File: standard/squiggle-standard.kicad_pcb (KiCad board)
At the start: 2 copper layers, 116 x 101.2 mm, 38 parts, among them SW1 switch, SW10 switch, SW11 switch, SW12 switch, SW13 switch, SW14 switch, SW15 switch, SW16 switch, SW17 switch, SW2 switch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

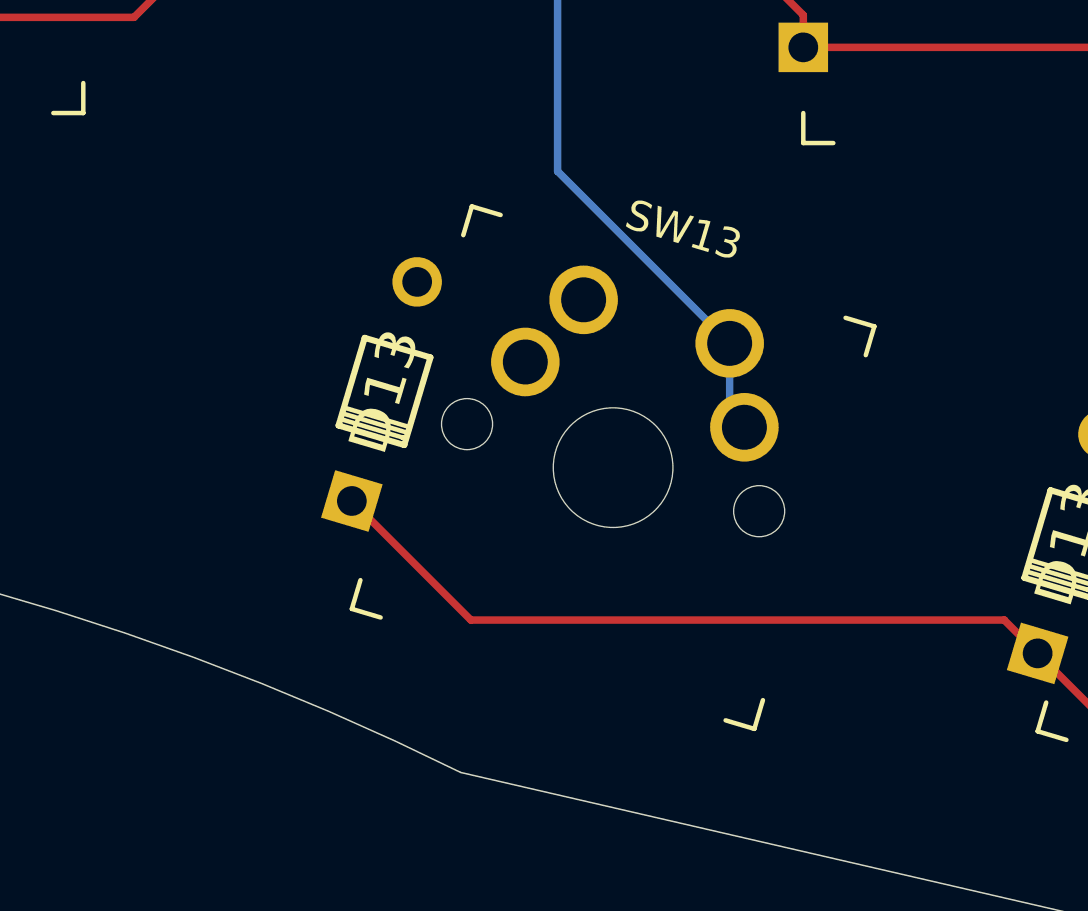
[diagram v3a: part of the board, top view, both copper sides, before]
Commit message: replaced switch with encoder
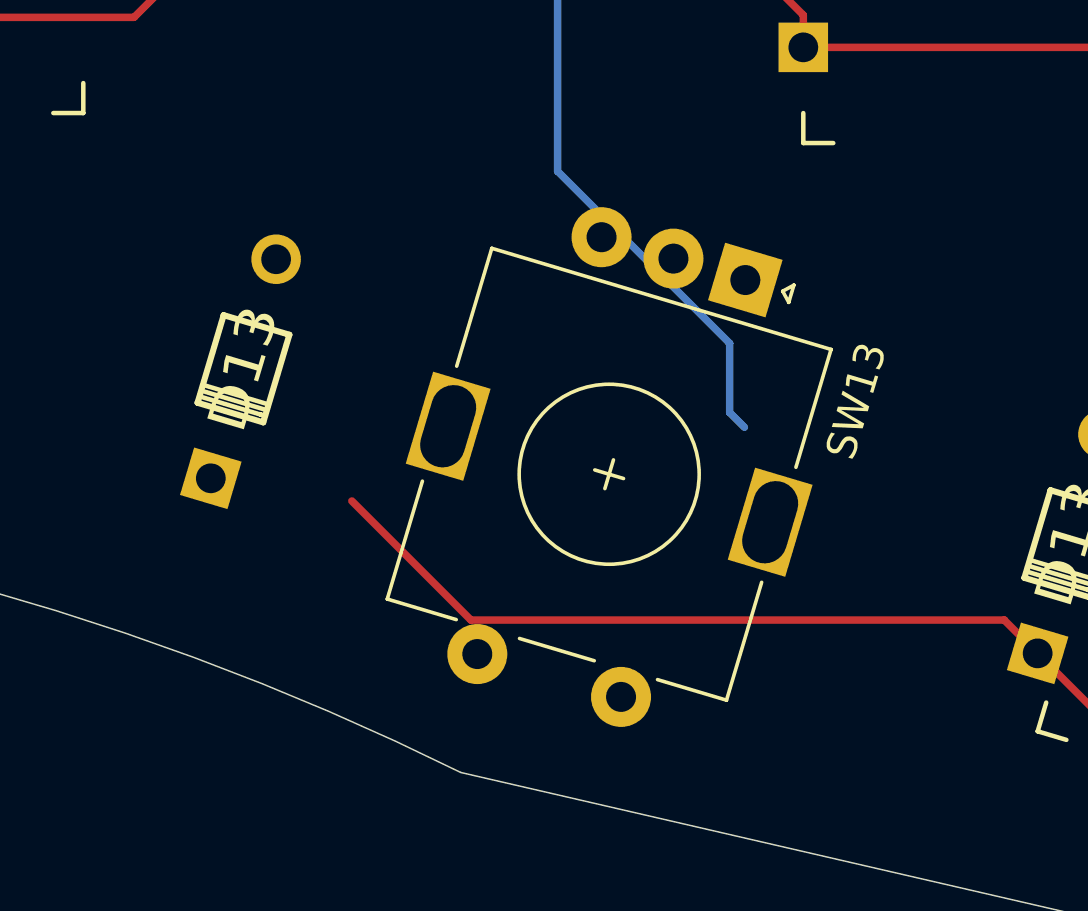
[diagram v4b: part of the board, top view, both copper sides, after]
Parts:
- SW13: footprint footprints:SW_MX_reversible -> Rotary_Encoder:RotaryEncoder_Alps_EC11E-Switch_Vertical_H20mm
- moved SW13 7.65 mm to (78.1, 77.6), turned to -106.6 degrees
- moved D13 4.76 mm to (61.3, 80.5)
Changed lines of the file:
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@@
       (net 11 "Net-(D15-Pad2)"))
   )
-  (footprint "footprints:SW_MX_reversible" (layer "F.Cu")
-    (at 73.66 83.82 -16.6)
-    (descr "MX-style keyswitch, reversible")
-    (tags "MX,cherry,gateron,kailh")
+  (footprint "Rotary_Encoder:RotaryEncoder_Alps_EC11E-Switch_Vertical_H20mm" (layer "F.Cu")
+    (at 78.067048 77.566382 -106.6)
+    (descr "Alps rotary encoder, EC12E... with switch, vertical shaft, http://www.alps.com/prod/info/E/HTML/Encoder/Incremental/EC11/EC11E15204A3.html")
+    (tags "rotary encoder")
     (attr through_hole)
-    (fp_text reference "SW13" (at 0 -8.255 -16.6) (layer "F.SilkS")
+    (fp_text reference "SW13" (at 2.8 -4.7 73.4) (layer "F.SilkS")
       (effects (font (size 1 1) (thickness 0.15)))
     )
-    (fp_text value "switch" (at 0 8.255 -16.6) (layer "F.Fab")
+    (fp_text value "switch" (at 7.5 10.4 73.4) (layer "F.Fab")
       (effects (font (size 1 1) (thickness 0.15)))
     )
-    (fp_text user "${REFERENCE}" (at 0 -8.255 -16.6) (layer "B.SilkS")
+    (fp_text user "2.00u" (at -15.24 8.255 73.4) (layer "Dwgs.User")
+      (effects (font (size 1.524 1.524) (thickness 0.3048)))
+    )
+    (fp_text user "${VALUE}" (at 0 8.255 73.4) (layer "B.Fab")
       (effects (font (size 1 1) (thickness 0.15)) (justify mirror))
     )
-    (fp_text user "2.00u" (at -15.24 8.255 163.4) (layer "Dwgs.User")
-      (effects (font (size 1.524 1.524) (thickness 0.3048)))
-    )
-    (fp_text user "${VALUE}" (at 0 8.255 -16.6) (layer "B.Fab")
-      (effects (font (size 1 1) (thickness 0.15)) (justify mirror))
-    )
-    (fp_text user "${REFERENCE}" (at 0 0 -16.6) (layer "B.Fab")
-      (effects (font (size 1 1) (thickness 0.15)) (justify mirror))
-    )
-    (fp_text user "${REFERENCE}" (at 0 0 -16.6) (layer "F.Fab")
+    (fp_text user "${REFERENCE}" (at 11.1 6.3 73.4) (layer "F.Fab")
       (effects (font (size 1 1) (thickness 0.15)))
     )
-    (fp_line (start -7 7) (end -7 6) (layer "B.SilkS") (width 0.15))
-    (fp_line (start -6 7) (end -7 7) (layer "B.SilkS") (width 0.15))
-    (fp_line (start 6 -7) (end 7 -7) (layer "B.SilkS") (width 0.15))
-    (fp_line (start 7 7) (end 6 7) (layer "B.SilkS") (width 0.15))
-    (fp_line (start 7 -7) (end 7 -6) (layer "B.SilkS") (width 0.15))
-    (fp_line (start -7 -7) (end -6 -7) (layer "B.SilkS") (width 0.15))
-    (fp_line (start 7 6) (end 7 7) (layer "B.SilkS") (width 0.15))
-    (fp_line (start -7 -6) (end -7 -7) (layer "B.SilkS") (width 0.15))
-    (fp_line (start 7 6) (end 7 7) (layer "F.SilkS") (width 0.15))
-    (fp_line (start -7 7) (end -7 6) (layer "F.SilkS") (width 0.15))
-    (fp_line (start -7 -6) (end -7 -7) (layer "F.SilkS") (width 0.15))
-    (fp_line (start -7 -7) (end -6 -7) (layer "F.SilkS") (width 0.15))
-    (fp_line (start -6 7) (end -7 7) (layer "F.SilkS") (width 0.15))
-    (fp_line (start 7 -7) (end 7 -6) (layer "F.SilkS") (width 0.15))
-    (fp_line (start 6 -7) (end 7 -7) (layer "F.SilkS") (width 0.15))
-    (fp_line (start 7 7) (end 6 7) (layer "F.SilkS") (width 0.15))
-    (fp_line (start -6.9 6.9) (end 6.9 6.9) (layer "Eco2.User") (width 0.15))
-    (fp_line (start 6.9 -6.9) (end 6.9 6.9) (layer "Eco2.User") (width 0.15))
-    (fp_line (start 6.9 -6.9) (end -6.9 -6.9) (layer "Eco2.User") (width 0.15))
-    (fp_line (start -6.9 6.9) (end -6.9 -6.9) (layer "Eco2.User") (width 0.15))
-    (fp_line (start -7.5 7.5) (end -7.5 -7.5) (layer "B.Fab") (width 0.15))
-    (fp_line (start -7.5 -7.5) (end 7.5 -7.5) (layer "B.Fab") (width 0.15))
-    (fp_line (start 7.5 7.5) (end -7.5 7.5) (layer "B.Fab") (width 0.15))
-    (fp_line (start 7.5 -7.5) (end 7.5 7.5) (layer "B.Fab") (width 0.15))
-    (fp_line (start 7.5 7.5) (end -7.5 7.5) (layer "F.Fab") (width 0.15))
-    (fp_line (start 7.5 -7.5) (end 7.5 7.5) (layer "F.Fab") (width 0.15))
-    (fp_line (start -7.5 -7.5) (end 7.5 -7.5) (layer "F.Fab") (width 0.15))
-    (fp_line (start -7.5 7.5) (end -7.5 -7.5) (layer "F.Fab") (width 0.15))
-    (pad "" np_thru_hole circle locked (at 0 0 343.4) (size 3.9878 3.9878) (drill 3.9878) (layers *.Cu *.Mask))
-    (pad "" np_thru_hole circle locked (at -5.08 0 343.4) (size 1.7018 1.7018) (drill 1.7018) (layers *.Cu *.Mask))
-    (pad "" np_thru_hole circle locked (at 5.08 0 343.4) (size 1.7018 1.7018) (drill 1.7018) (layers *.Cu *.Mask))
-    (pad "1" thru_hole circle locked (at -3.81 -2.54 343.4) (size 2.286 2.286) (drill 1.4986) (layers *.Cu *.Mask)
-      (net 8 "Net-(D10-Pad2)"))
-    (pad "1" thru_hole circle locked (at -2.54 -5.08 343.4) (size 2.286 2.286) (drill 1.4986) (layers *.Cu *.Mask)
-      (net 8 "Net-(D10-Pad2)"))
-    (pad "2" thru_hole circle locked (at 3.809999 -2.54 343.4) (size 2.286 2.286) (drill 1.4986) (layers *.Cu *.Mask)
-      (net 18 "COL2"))
-    (pad "2" thru_hole circle locked (at 2.54 -5.08 343.4) (size 2.286 2.286) (drill 1.4986) (layers *.Cu *.Mask)
-      (net 18 "COL2"))
+    (fp_line (start 13.6 8.4) (end 9.5 8.4) (layer "F.SilkS") (width 0.12))
+    (fp_line (start 7 2.5) (end 8 2.5) (layer "F.SilkS") (width 0.12))
+    (fp_line (start 0.3 -1.6) (end 0 -1.3) (layer "F.SilkS") (width 0.12))
+    (fp_line (start -0.3 -1.6) (end 0.3 -1.6) (layer "F.SilkS") (width 0.12))
+    (fp_line (start 5.5 8.4) (end 1.4 8.4) (layer "F.SilkS") (width 0.12))
+    (fp_line (start 5.5 -3.4) (end 1.4 -3.4) (layer "F.SilkS") (width 0.12))
+    (fp_line (start 13.6 6) (end 13.6 8.4) (layer "F.SilkS") (width 0.12))
+    (fp_line (start 13.6 -3.4) (end 13.6 -1) (layer "F.SilkS") (width 0.12))
+    (fp_line (start 9.5 -3.4) (end 13.6 -3.4) (layer "F.SilkS") (width 0.12))
+    (fp_line (start 0 -1.3) (end -0.3 -1.6) (layer "F.SilkS") (width 0.12))
+    (fp_line (start 7.5 2) (end 7.5 3) (layer "F.SilkS") (width 0.12))
+    (fp_line (start 1.4 -3.4) (end 1.4 8.4) (layer "F.SilkS") (width 0.12))
+    (fp_line (start 13.6 1.2) (end 13.6 3.8) (layer "F.SilkS") (width 0.12))
+    (fp_circle (center 7.5 2.5) (end 10.5 2.5) (layer "F.SilkS") (width 0.12) (fill none))
+    (fp_line (start 16 9.6) (end -1.5 9.6) (layer "F.CrtYd") (width 0.05))
+    (fp_line (start -1.5 -4.6) (end -1.5 9.6) (layer "F.CrtYd") (width 0.05))
+    (fp_line (start -1.5 -4.6) (end 16 -4.6) (layer "F.CrtYd") (width 0.05))
+    (fp_line (start 16 9.6) (end 16 -4.6) (layer "F.CrtYd") (width 0.05))
+    (fp_line (start 2.5 -3.3) (end 13.5 -3.3) (layer "F.Fab") (width 0.12))
+    (fp_line (start 13.5 8.3) (end 1.5 8.3) (layer "F.Fab") (width 0.12))
+    (fp_line (start 1.5 -2.2) (end 2.5 -3.3) (layer "F.Fab") (width 0.12))
+    (fp_line (start 1.5 8.3) (end 1.5 -2.2) (layer "F.Fab") (width 0.12))
+    (fp_line (start 7.5 -0.5) (end 7.5 5.5) (layer "F.Fab") (width 0.12))
+    (fp_line (start 4.5 2.5) (end 10.5 2.5) (layer "F.Fab") (width 0.12))
+    (fp_line (start 13.5 -3.3) (end 13.5 8.3) (layer "F.Fab") (width 0.12))
+    (fp_circle (center 7.5 2.5) (end 10.5 2.5) (layer "F.Fab") (width 0.12) (fill none))
+    (pad "A" thru_hole rect (at 0 0 253.4) (size 2 2) (drill 1) (layers *.Cu *.Mask))
+    (pad "B" thru_hole circle (at 0 5 253.4) (size 2 2) (drill 1) (layers *.Cu *.Mask))
+    (pad "C" thru_hole circle (at 0 2.5 253.4) (size 2 2) (drill 1) (layers *.Cu *.Mask))
+    (pad "MP" thru_hole rect (at 7.5 -3.1 253.4) (size 3.2 2) (drill oval 2.8 1.5) (layers *.Cu *.Mask))
+    (pad "MP" thru_hole rect (at 7.5 8.1 253.4) (size 3.2 2) (drill oval 2.8 1.5) (layers *.Cu *.Mask))
+    (pad "S1" thru_hole circle (at 14.5 5 253.4) (size 2 2) (drill 1) (layers *.Cu *.Mask))
+    (pad "S2" thru_hole circle (at 14.5 0 253.4) (size 2 2) (drill 1) (layers *.Cu *.Mask))
+    (model "${KICAD6_3DMODEL_DIR}/Rotary_Encoder.3dshapes/RotaryEncoder_Alps_EC11E-Switch_Vertical_H20mm.wrl"
+      (offset (xyz 0 0 0))
+      (scale (xyz 1 1 1))
+      (rotate (xyz 0 0 0))
+    )
   )
   (footprint "footprints:diode" (layer "F.Cu")
-    (at 66.04 81.28 -106.6)
+    (at 61.338473 80.523791 -106.6)
     (attr through_hole)
     (fp_text reference "D13" (at 0 0 73.4) (layer "F.SilkS")
